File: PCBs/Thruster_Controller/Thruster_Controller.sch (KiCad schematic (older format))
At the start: 41 parts, among them J1 PHASE_A, J2 PHASE_B, J3 PHASE_C, J4 Conn_01x01, J5 Pogo Conn, J6 Conn_01x01, J7 Conn_01x01, J8 Conn_01x01, U2 RTQ2569-50GQW, U3 MCP2515, U4 TPS62172DSGR, U8 MCP2562, Y1 20MHz

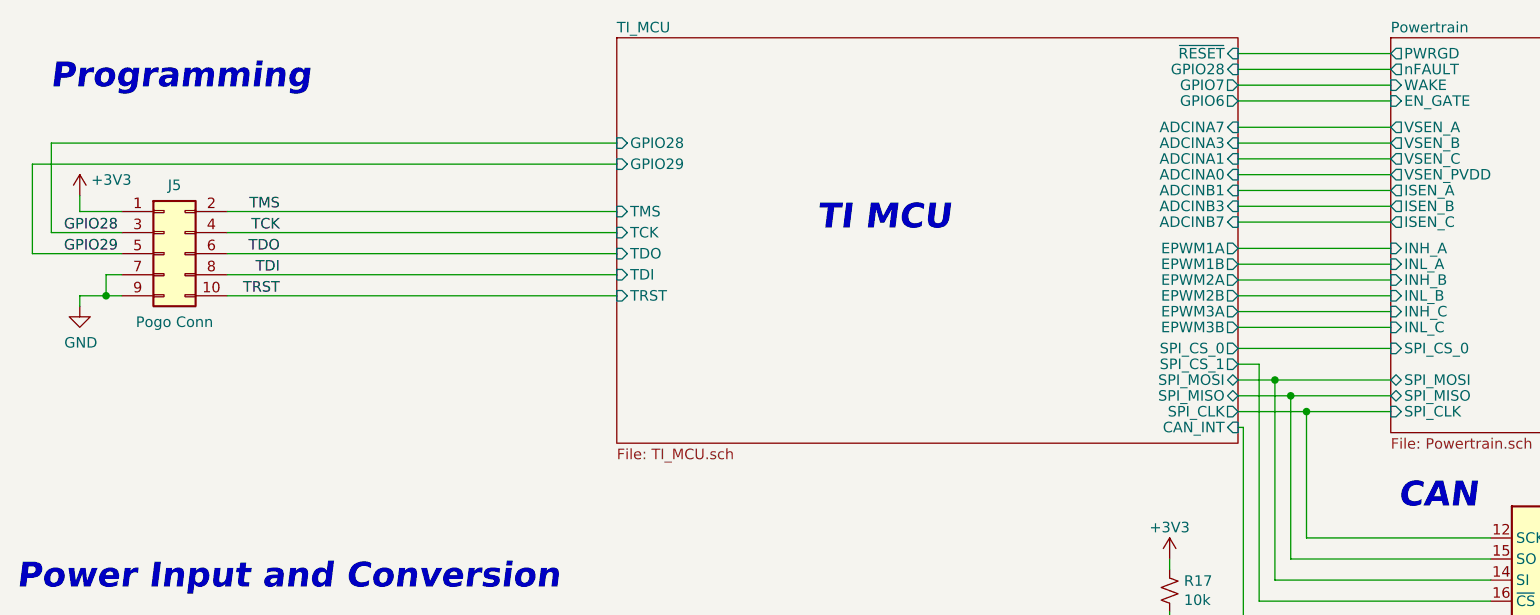
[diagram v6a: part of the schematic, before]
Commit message: BOM and Small Changes
- Created BOM
- Small routing cleanups
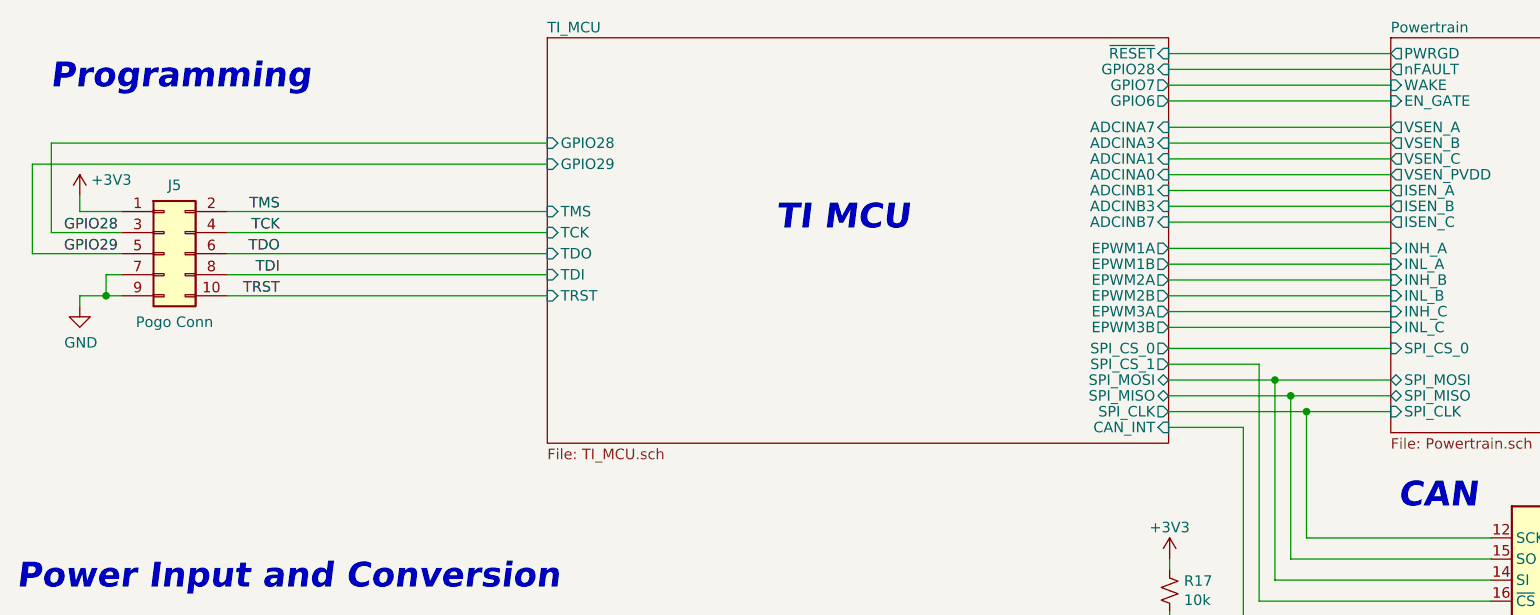
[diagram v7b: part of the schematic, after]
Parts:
- C21: Digikey 311-1060-1-ND -> 732-7456-1-ND
- R7: Digikey P2.7KDACT-ND -> RMCF0603JT2K70CT-ND
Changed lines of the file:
@@
 Comment4 ""
 $EndDescr
-Text Notes 4450 2375 0    118  Italic 24
+Text Notes 4255 2375 0    118  Italic 24
 TI MCU
 Text Notes 8025 2350 0    118  Italic 24
@@
 $EndComp
 Wire Wire Line
-	6450 1525 7175 1525
-Wire Wire Line
-	7175 1600 6450 1600
-Wire Wire Line
-	6450 1675 7175 1675
-Wire Wire Line
-	7175 1750 6450 1750
-Wire Wire Line
-	6450 1875 7175 1875
-Wire Wire Line
-	7175 1950 6450 1950
-Wire Wire Line
-	6450 2025 7175 2025
-Wire Wire Line
-	7175 2100 6450 2100
-Wire Wire Line
-	6450 2175 7175 2175
-Wire Wire Line
-	7175 2250 6450 2250
-Wire Wire Line
-	6450 2325 7175 2325
-Wire Wire Line
-	7175 2450 6450 2450
-Wire Wire Line
-	6450 2525 7175 2525
-Wire Wire Line
-	7175 2600 6450 2600
-Wire Wire Line
-	6450 2675 7175 2675
-Wire Wire Line
-	7175 2750 6450 2750
-Wire Wire Line
-	6450 2825 7175 2825
-Wire Wire Line
-	7175 2925 6450 2925
-Wire Wire Line
-	6450 3075 6625 3075
+	6120 1525 7175 1525
+Wire Wire Line
+	7175 1600 6120 1600
+Wire Wire Line
+	6120 1675 7175 1675
+Wire Wire Line
+	7175 1750 6120 1750
+Wire Wire Line
+	6120 1875 7175 1875
+Wire Wire Line
+	7175 1950 6120 1950
+Wire Wire Line
+	6120 2025 7175 2025
+Wire Wire Line
+	7175 2100 6120 2100
+Wire Wire Line
+	6120 2175 7175 2175
+Wire Wire Line
+	7175 2250 6120 2250
+Wire Wire Line
+	6120 2325 7175 2325
+Wire Wire Line
+	7175 2450 6120 2450
+Wire Wire Line
+	6120 2525 7175 2525
+Wire Wire Line
+	7175 2600 6120 2600
+Wire Wire Line
+	6120 2675 7175 2675
+Wire Wire Line
+	7175 2750 6120 2750
+Wire Wire Line
+	6120 2825 7175 2825
+Wire Wire Line
+	7175 2925 6120 2925
+Wire Wire Line
+	6120 3075 6625 3075
 Wire Wire Line
 	7175 3150 6700 3150
 Wire Wire Line
-	6450 3225 6775 3225
+	6120 3225 6775 3225
 $Comp
 L Connector_Generic:Conn_02x05_Odd_Even J5
@@
 TRST
 Wire Wire Line
-	6450 3000 6550 3000
+	6120 3000 6550 3000
 Wire Wire Line
 	6550 3000 6550 4125
@@
 Connection ~ 6700 3150
 Wire Wire Line
-	6700 3150 6450 3150
+	6700 3150 6120 3150
 Wire Wire Line
 	6775 3225 6775 3825
@@
 	6775 3225 7175 3225
 $Sheet
-S 3500 1450 2950 1925
+S 3170 1450 2950 1925
 U 5E20A372
 F0 "TI_MCU" 50
 F1 "TI_MCU.sch" 50
-F2 "GPIO28" I R 6450 1600 50
-F3 "SPI_CLK" O R 6450 3225 50
-F4 "ADCINA7" I R 6450 1875 50
-F5 "ADCINA3" I R 6450 1950 50
-F6 "ADCINA1" I R 6450 2025 50
-F7 "ADCINA0" I R 6450 2100 50
-F8 "ADCINB1" I R 6450 2175 50
-F9 "ADCINB3" I R 6450 2250 50
-F10 "ADCINB7" I R 6450 2325 50
-F11 "EPWM1A" O R 6450 2450 50
-F12 "EPWM1B" O R 6450 2525 50
-F13 "EPWM2A" O R 6450 2600 50
-F14 "EPWM2B" O R 6450 2675 50
-F15 "EPWM3A" O R 6450 2750 50
-F16 "EPWM3B" O R 6450 2825 50
-F17 "SPI_CS_0" O R 6450 2925 50
-F18 "~RESET~" I R 6450 1525 50
-F19 "SPI_MOSI" B R 6450 3075 50
-F20 "SPI_MISO" B R 6450 3150 50
-F21 "GPIO6" O R 6450 1750 50
-F22 "GPIO7" O R 6450 1675 50
-F23 "GPIO29" I L 3500 2050 50
-F24 "TRST" I L 3500 2675 50
-F25 "TCK" I L 3500 2375 50
-F26 "TMS" I L 3500 2275 50
-F27 "TDI" I L 3500 2575 50
-F28 "TDO" I L 3500 2475 50
-F29 "GPIO28" I L 3500 1950 50
-F30 "SPI_CS_1" O R 6450 3000 50
-F31 "CAN_INT" I R 6450 3300 50
+F2 "GPIO28" I R 6120 1600 50
+F3 "SPI_CLK" O R 6120 3225 50
+F4 "ADCINA7" I R 6120 1875 50
+F5 "ADCINA3" I R 6120 1950 50
+F6 "ADCINA1" I R 6120 2025 50
+F7 "ADCINA0" I R 6120 2100 50
+F8 "ADCINB1" I R 6120 2175 50
+F9 "ADCINB3" I R 6120 2250 50
+F10 "ADCINB7" I R 6120 2325 50
+F11 "EPWM1A" O R 6120 2450 50
+F12 "EPWM1B" O R 6120 2525 50
+F13 "EPWM2A" O R 6120 2600 50
+F14 "EPWM2B" O R 6120 2675 50
+F15 "EPWM3A" O R 6120 2750 50
+F16 "EPWM3B" O R 6120 2825 50
+F17 "SPI_CS_0" O R 6120 2925 50
+F18 "~RESET~" I R 6120 1525 50
+F19 "SPI_MOSI" B R 6120 3075 50
+F20 "SPI_MISO" B R 6120 3150 50
+F21 "GPIO6" O R 6120 1750 50
+F22 "GPIO7" O R 6120 1675 50
+F23 "GPIO29" I L 3170 2050 50
+F24 "TRST" I L 3170 2675 50
+F25 "TCK" I L 3170 2375 50
+F26 "TMS" I L 3170 2275 50
+F27 "TDI" I L 3170 2575 50
+F28 "TDO" I L 3170 2475 50
+F29 "GPIO28" I L 3170 1950 50
+F30 "SPI_CS_1" O R 6120 3000 50
+F31 "CAN_INT" I R 6120 3300 50
 $EndSheet
 $Comp
@@
 	9000 4600 9000 4625
 Wire Wire Line
-	6450 3300 6475 3300
+	6120 3300 6475 3300
 Wire Wire Line
 	6475 3300 6475 4275
@@
 F 2 "Capacitors_SMD:C_0402" H 6950 4450 50  0001 C CNN
 F 3 "~" H 6950 4450 50  0001 C CNN
-F 4 "311-1060-1-ND" V 6950 4450 50  0001 C CNN "Digikey"
+F 4 "732-7456-1-ND" V 6950 4450 50  0001 C CNN "Digikey"
 	1    6950 4450
 	0    1    1    0
@@
 	10050 2000 10400 2000
 Wire Wire Line
-	1650 2275 3500 2275
-Wire Wire Line
-	1650 2375 3500 2375
-Wire Wire Line
-	1650 2475 3500 2475
-Wire Wire Line
-	1650 2575 3500 2575
-Wire Wire Line
-	1650 2675 3500 2675
+	1650 2275 3170 2275
+Wire Wire Line
+	1650 2375 3170 2375
+Wire Wire Line
+	1650 2475 3170 2475
+Wire Wire Line
+	1650 2575 3170 2575
+Wire Wire Line
+	1650 2675 3170 2675
 $Comp
 L Connector_Generic:Conn_01x01 J6
@@
 F 2 "Resistors_SMD:R_0603" V 3295 6665 50  0001 C CNN
 F 3 "~" H 3255 6675 50  0001 C CNN
-F 4 "P2.7KDACT-ND" H 3255 6675 50  0001 C CNN "Digikey"
+F 4 "RMCF0603JT2K70CT-ND" H 3255 6675 50  0001 C CNN "Digikey"
 	1    3255 6675
 	1    0    0    -1
@@
 	815  2375 1150 2375
 Wire Wire Line
-	815  1950 3500 1950
+	815  1950 3170 1950
 Wire Wire Line
 	725  2475 725  2050
@@
 	725  2475 1150 2475
 Wire Wire Line
-	725  2050 3500 2050
+	725  2050 3170 2050
 $Comp
 L Connector:TestPoint TP1
@@
 	3640 6125 3640 6075
 $Comp
-L power:+5V #PWR?
+L power:+5V #PWR0154
 U 1 1 5EBB5551
 P 3640 6075
-F 0 "#PWR?" H 3640 5925 50  0001 C CNN
+F 0 "#PWR0154" H 3640 5925 50  0001 C CNN
 F 1 "+5V" H 3640 6225 50  0000 C CNN
 F 2 "" H 3640 6075 50  0001 C CNN

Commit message: BOM Changes
- Found cheaper alternatives for some components
- Changed sizing of some components to reduce cost where possible
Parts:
- C49: Digikey 490-5523-1-ND -> 1276-6454-1-ND
- C50: footprint Capacitors_SMD:C_0603 -> Capacitors_SMD:C_0805; Digikey 490-7611-1-ND -> 1276-1100-1-ND
- R19: footprint Resistors_SMD:R_0603 -> Resistors_SMD:R_0805; Digikey RHM330DCT-ND -> 2019-RK73B2ATTD331JCT-ND
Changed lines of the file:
@@
 F 2 "Capacitors_SMD:C_0805" H 1125 5675 50  0001 C CNN
 F 3 "" H 1125 5675 50  0001 C CNN
-F 4 "490-5523-1-ND" H 1125 5675 50  0001 C CNN "Digikey"
+F 4 "1276-6454-1-ND" H 1125 5675 50  0001 C CNN "Digikey"
 F 5 "25V" H 1005 5525 50  0000 C CNN "Voltage"
 	1    1125 5675
@@
 F 0 "C50" H 2735 5690 50  0000 L CNN
 F 1 "22uF" H 2745 5535 50  0000 L CNN
-F 2 "Capacitors_SMD:C_0603" H 2700 5620 50  0001 C CNN
+F 2 "Capacitors_SMD:C_0805" H 2700 5620 50  0001 C CNN
 F 3 "" H 2700 5620 50  0001 C CNN
-F 4 "490-7611-1-ND" H 2700 5620 50  0001 C CNN "Digikey"
+F 4 "1276-1100-1-ND" H 2700 5620 50  0001 C CNN "Digikey"
 	1    2700 5620
 	1    0    0    -1
@@
 F 0 "R19" H 4045 6670 50  0000 L CNN
 F 1 "330" H 4045 6595 50  0000 L CNN
-F 2 "Resistors_SMD:R_0603" V 4035 6660 50  0001 C CNN
+F 2 "Resistors_SMD:R_0805" V 4035 6660 50  0001 C CNN
 F 3 "~" H 3995 6670 50  0001 C CNN
-F 4 "RHM330DCT-ND" H 3995 6670 50  0001 C CNN "Digikey"
+F 4 "2019-RK73B2ATTD331JCT-ND" H 3995 6670 50  0001 C CNN "Digikey"
 	1    3995 6670
 	1    0    0    -1
